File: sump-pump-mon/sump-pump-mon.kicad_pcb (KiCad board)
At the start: 2 copper layers, 95.3 x 58.4 mm, 40 parts, among them J1 Main Input, J2 Wall Power, J3 Battery, J4 Display_Conn, J5 Aux Input, J6 I2C, J7 I2C Stemma, J8 I2C Stemma QT, SW3 MODE, SW4 POWER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

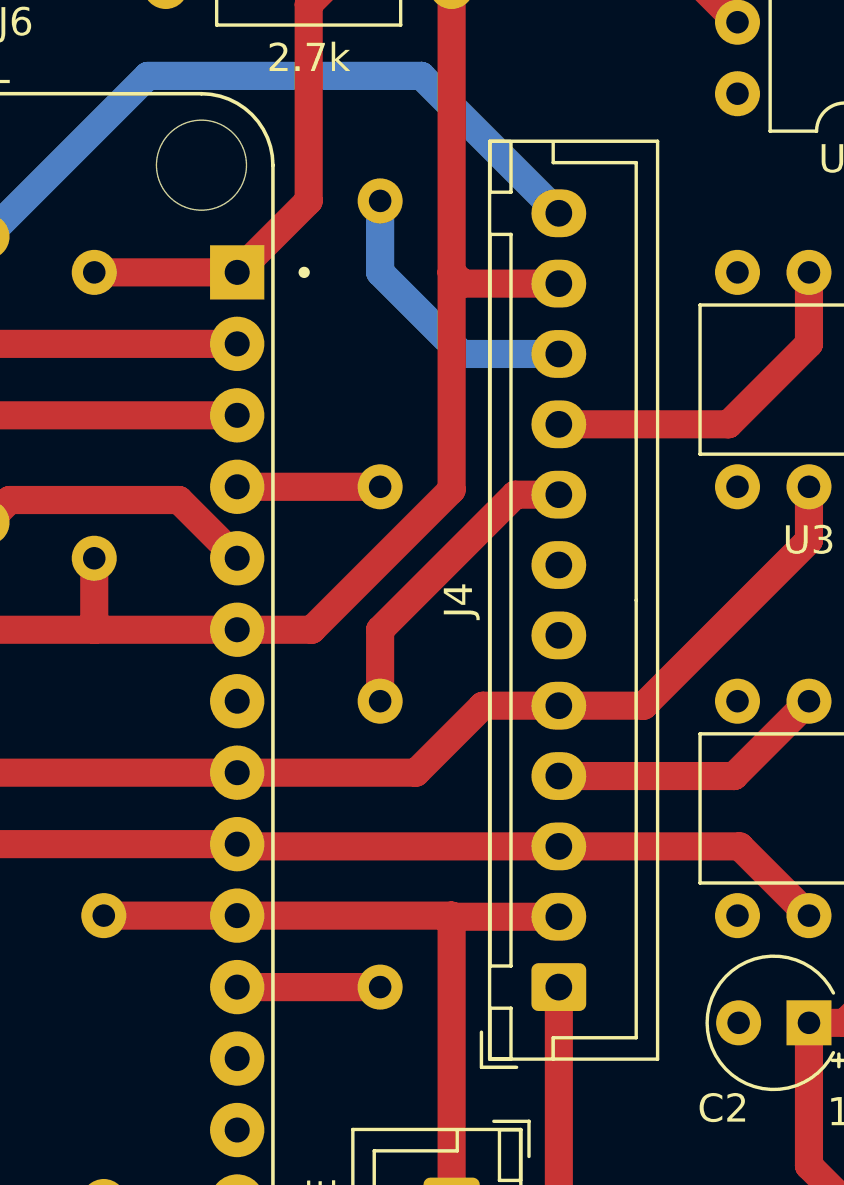
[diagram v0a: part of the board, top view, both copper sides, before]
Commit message: updated silkscreen & renamed nets
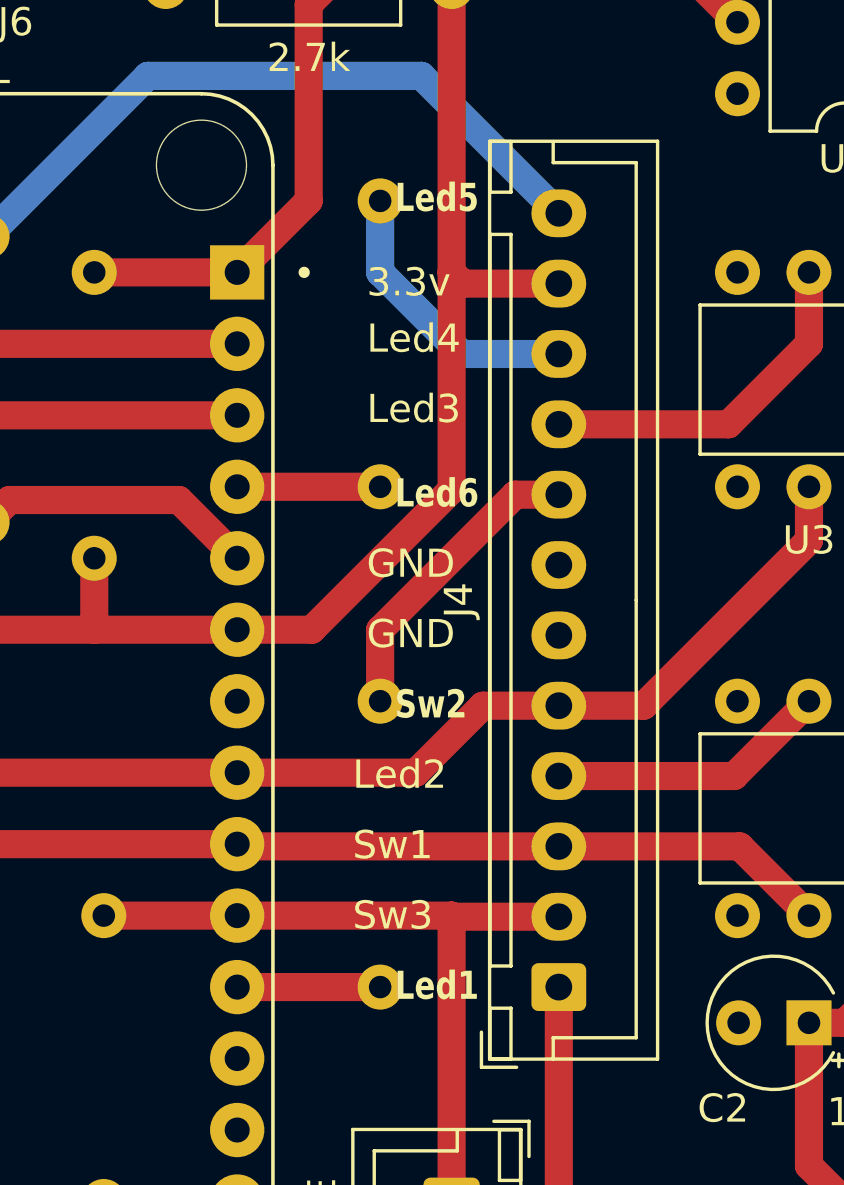
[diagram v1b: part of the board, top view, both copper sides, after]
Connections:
- net Aux_Input renamed Yellow_Button
- net Main_Input renamed Green_Button
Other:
- board text added: "3.3v"
- board text added: "Led1"
- board text added: "Led2"
- board text added: "Led3"
- board text added: "Led4"
- board text added: "Led5"
- board text added: "Led6"
- board text added: "Sw1"
- board text added: "Sw2"
- board text added: "Sw3"
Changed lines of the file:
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@@
 	(net 20 "GND")
 	(net 21 "Net-(A1B-D2)")
-	(net 22 "Aux_Input")
-	(net 23 "Main_Input")
+	(net 22 "Yellow_Button")
+	(net 23 "Green_Button")
 	(net 24 "LED_6V")
 	(net 25 "unconnected-(U2-Pad6)")
@@
 			(layers "*.Cu" "*.Mask")
 			(remove_unused_layers no)
-			(net 23 "Main_Input")
+			(net 23 "Green_Button")
 			(pintype "passive")
 		)
@@
 			(layers "*.Cu" "*.Mask")
 			(remove_unused_layers no)
-			(net 22 "Aux_Input")
+			(net 22 "Yellow_Button")
 			(pinfunction "D5")
 			(pintype "bidirectional")
@@
 			(layers "*.Cu" "*.Mask")
 			(remove_unused_layers no)
-			(net 23 "Main_Input")
+			(net 23 "Green_Button")
 			(pinfunction "D6")
 			(pintype "bidirectional")
@@
 			(layers "*.Cu" "*.Mask")
 			(remove_unused_layers no)
-			(net 23 "Main_Input")
+			(net 23 "Green_Button")
 			(pinfunction "Pin_3")
 			(pintype "passive")
@@
 			(layers "*.Cu" "*.Mask")
 			(remove_unused_layers no)
-			(net 22 "Aux_Input")
+			(net 22 "Yellow_Button")
 			(pinfunction "Pin_5")
 			(pintype "passive")
@@
 			(layers "*.Cu" "*.Mask")
 			(remove_unused_layers no)
-			(net 22 "Aux_Input")
+			(net 22 "Yellow_Button")
 			(pintype "passive")
 		)
@@
 			(layers "*.Cu" "*.Mask")
 			(remove_unused_layers no)
-			(net 22 "Aux_Input")
+			(net 22 "Yellow_Button")
 			(pintype "passive")
 		)
@@
 			(layers "*.Cu" "*.Mask")
 			(remove_unused_layers no)
-			(net 23 "Main_Input")
+			(net 23 "Green_Button")
 			(pintype "passive")
 		)
@@
 		)
 	)
+	(gr_text "GND"
+		(at 157 49 0)
+		(layer "F.SilkS")
+		(effects
+			(font
+				(size 1 1)
+				(thickness 0.15)
+			)
+			(justify left bottom)
+		)
+	)
 	(gr_text "Vin"
 		(at 119.38 51.054 270)
@@
 		)
 	)
+	(gr_text "3.3v"
+		(at 157 36.5 0)
+		(layer "F.SilkS")
+		(effects
+			(font
+				(size 1 1)
+				(thickness 0.15)
+			)
+			(justify left bottom)
+		)
+	)
 	(gr_text "+"
 		(at 205.232 53.086 90)
@@
 		)
 	)
+	(gr_text "Led3"
+		(at 157 41 0)
+		(layer "F.SilkS")
+		(effects
+			(font
+				(size 1 1)
+				(thickness 0.15)
+			)
+			(justify left bottom)
+		)
+	)
 	(gr_text "-\n"
 		(at 210.312 60.96 180)
@@
 		)
 	)
+	(gr_text "Led2\n"
+		(at 156.5 54 0)
+		(layer "F.SilkS")
+		(effects
+			(font
+				(size 1 1)
+				(thickness 0.15)
+			)
+			(justify left bottom)
+		)
+	)
+	(gr_text "GND"
+		(at 157 46.5 0)
+		(layer "F.SilkS")
+		(effects
+			(font
+				(size 1 1)
+				(thickness 0.15)
+			)
+			(justify left bottom)
+		)
+	)
+	(gr_text "Led5"
+		(at 158 33.5 0)
+		(layer "F.SilkS")
+		(effects
+			(font
+				(size 1 0.8)
+				(thickness 0.15)
+				(bold yes)
+			)
+			(justify left bottom)
+		)
+	)
 	(gr_text "BATT"
 		(at 205.486 53.086 0)
@@
 		)
 	)
+	(gr_text "Sw1"
+		(at 156.5 56.5 0)
+		(layer "F.SilkS")
+		(effects
+			(font
+				(size 1 1)
+				(thickness 0.15)
+			)
+			(justify left bottom)
+		)
+	)
+	(gr_text "Led4"
+		(at 157 38.5 0)
+		(layer "F.SilkS")
+		(effects
+			(font
+				(size 1 1)
+				(thickness 0.15)
+			)
+			(justify left bottom)
+		)
+	)
 	(gr_text "AUX"
 		(at 202.438 47.244 90)
@@
 		)
 	)
+	(gr_text "Sw3"
+		(at 156.5 59 0)
+		(layer "F.SilkS")
+		(effects
+			(font
+				(size 1 1)
+				(thickness 0.15)
+			)
+			(justify left bottom)
+		)
+	)
 	(gr_text "+\n"
 		(at 203.962 62.23 0)
@@
 		)
 	)
+	(gr_text "Led1\n"
+		(at 158 61.5 0)
+		(layer "F.SilkS")
+		(effects
+			(font
+				(size 1 0.8)
+				(thickness 0.15)
+				(bold yes)
+			)
+			(justify left bottom)
+		)
+	)
+	(gr_text "Led6"
+		(at 158 44 0)
+		(layer "F.SilkS")
+		(effects
+			(font
+				(size 1 0.8)
+				(thickness 0.15)
+				(bold yes)
+			)
+			(justify left bottom)
+		)
+	)
+	(gr_text "Sw2"
+		(at 158 51.5 0)
+		(layer "F.SilkS")
+		(effects
+			(font
+				(size 1 0.8)
+				(thickness 0.15)
+				(bold yes)
+			)
+			(justify left bottom)
+		)
+	)
